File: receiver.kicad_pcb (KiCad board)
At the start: 2 copper layers, 63 x 61 mm, 35 parts, among them J1 Screw_Terminal_01x02, J2 Screw_Terminal_01x02, Q1 BC549, Q2 BC549, U1 AMS1117-3.3

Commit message: Почти готово. Осталось добавить переменный конденсатор
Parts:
- moved C8 56.9 mm to (76.0, 90.1), turned to 0 degrees
- moved C11 53.1 mm to (76.0, 86.0), turned to 0 degrees
- moved D1 51.1 mm to (124.7, 97.8), turned to -90 degrees
- moved C9 39.5 mm to (112.0, 96.6), turned to 90 degrees
- moved R1 37.6 mm to (89.8, 100.4), turned to 180 degrees
- moved C2 35.6 mm to (107.7, 61.2), turned to -90 degrees
- moved C4 35.1 mm to (108.2, 96.8), turned to 180 degrees
- moved D2 25.4 mm to (92.5, 91.0)
- moved C7 23.3 mm to (115.6, 81.5), turned to -90 degrees
- moved R2 23.2 mm to (89.8, 98.0), turned to 0 degrees
- moved D3 23.0 mm to (75.5, 99.4)
- moved C14 22.9 mm to (85.3, 81.7), turned to 180 degrees
- moved C15 22.2 mm to (99.5, 86.3), turned to 0 degrees
- moved C5 19.2 mm to (108.3, 93.3), turned to 180 degrees
- moved C12 15.8 mm to (86.2, 94.0), turned to 180 degrees
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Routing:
- net Net-(D3-K): track 7.52 -> 111.2 mm
- net Net-(C10-Pad1): track 24.7 -> 103.8 mm, vias 0 -> 2
- net Net-(AE1-A): track 15.8 -> 82.4 mm
- net Net-(D1-K): track 21.9 -> 77.2 mm
- net Earth: track 80.8 -> 134.6 mm
- net Net-(C12-Pad1): track 43.4 -> 3.82 mm
- net Net-(D2-input): track 0.00 -> 36.5 mm
- net Net-(D2-MUX): track 18.4 -> 45.8 mm
- net Net-(C7-Pad2): track 0.00 -> 25.9 mm
- net Net-(C13-Pad2): track 33.4 -> 10.0 mm, vias 2 -> 0
- net Net-(D2-OSC): track 16.4 -> 37.4 mm, vias 2 -> 0
- net Net-(C9-Pad2): track 0.00 -> 19.4 mm
- net Net-(C12-Pad2): track 32.0 -> 14.3 mm
- net Net-(D2-fld): track 17.8 -> 8.96 mm
- net +3V3: track 194.6 -> 188.3 mm, vias 0 -> 3
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
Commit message: Почти все. Четыре дорожки внутри микросхемы. Это много.
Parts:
- moved C5 10.1 mm to (98.3, 91.6), turned to 0 degrees
- moved C4 10.1 mm to (98.3, 95.1), turned to 0 degrees
- moved C18 8.39 mm to (111.8, 67.4)
- moved C7 7.28 mm to (116.0, 74.3)
- moved C9 7.28 mm to (112.4, 89.4)
- moved C10 7.25 mm to (108.1, 88.5)
- moved C1 4.55 mm to (119.0, 63.7)
- moved C11 3.08 mm to (75.8, 89.1)
- moved C14 3.08 mm to (85.1, 84.8)
- moved C8 3.08 mm to (75.8, 93.2)
- moved C12 3.08 mm to (86.0, 97.1)
- moved D1 2.57 mm to (124.7, 95.2)
- moved AE1 2.52 mm to (130.6, 100.8)
- moved R4 2.41 mm to (130.3, 60.4)
- moved D4 2.12 mm to (108.6, 54.6)
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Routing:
- net +3V3: track 188.3 -> 212.4 mm, vias 3 -> 4
- net Net-(C7-Pad2): track 25.9 -> 49.8 mm
- net Net-(C10-Pad1): track 103.8 -> 80.7 mm
- net Net-(D3-K): track 111.2 -> 96.0 mm
- net Net-(D1-K): track 77.2 -> 62.3 mm
- net Earth: track 134.6 -> 125.0 mm
- net Net-(J2-Pin_1): track 11.8 -> 18.8 mm
- net Net-(C9-Pad2): track 19.4 -> 25.0 mm
- net Net-(C14-Pad1): track 11.3 -> 6.84 mm
- net Net-(D2-MUX): track 45.8 -> 48.9 mm
- net Net-(D2-OSC): track 37.4 -> 39.9 mm
- net Net-(C12-Pad2): track 14.3 -> 16.6 mm
- net Net-(D2-input): track 36.5 -> 34.6 mm
- net Net-(Q1-B): track 5.72 -> 7.19 mm
- net Net-(C12-Pad1): track 3.82 -> 5.14 mm
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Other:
- outline, holes or cut-outs redrawn

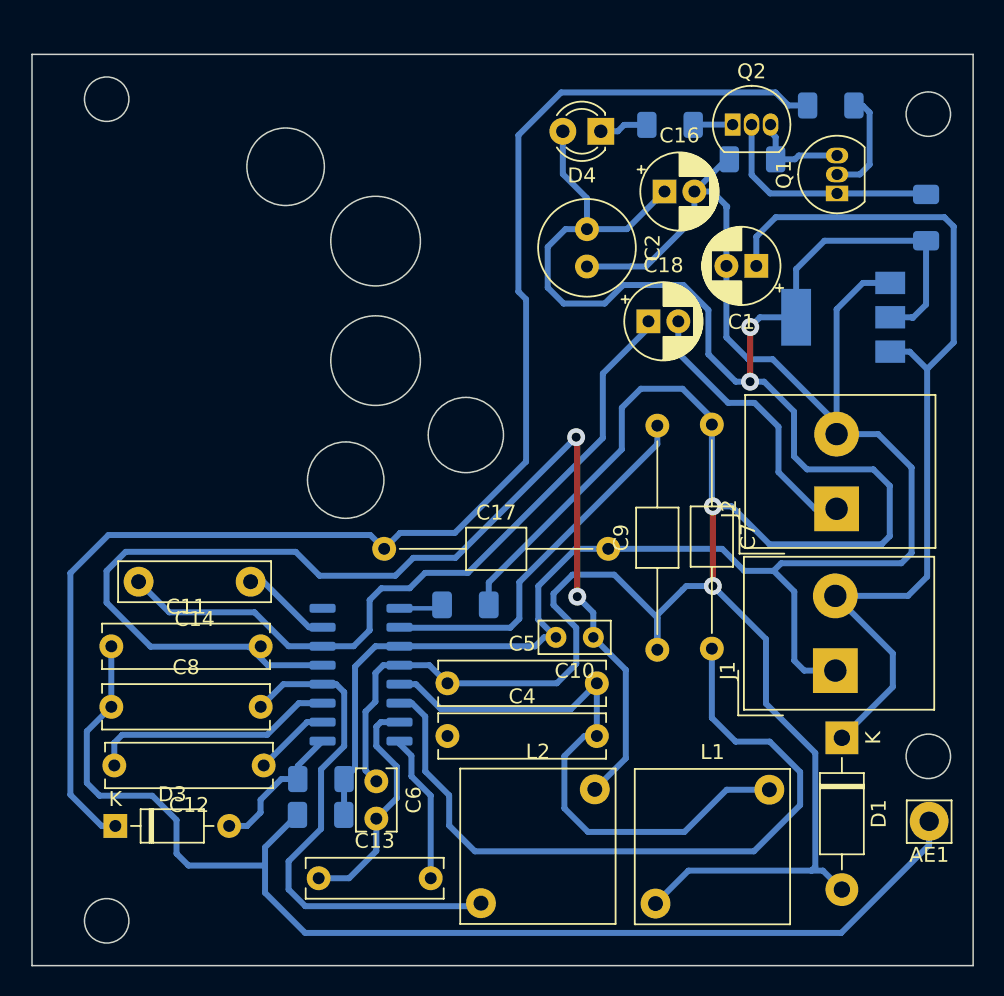
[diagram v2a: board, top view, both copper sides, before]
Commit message: Уменьшена плотность дорожек
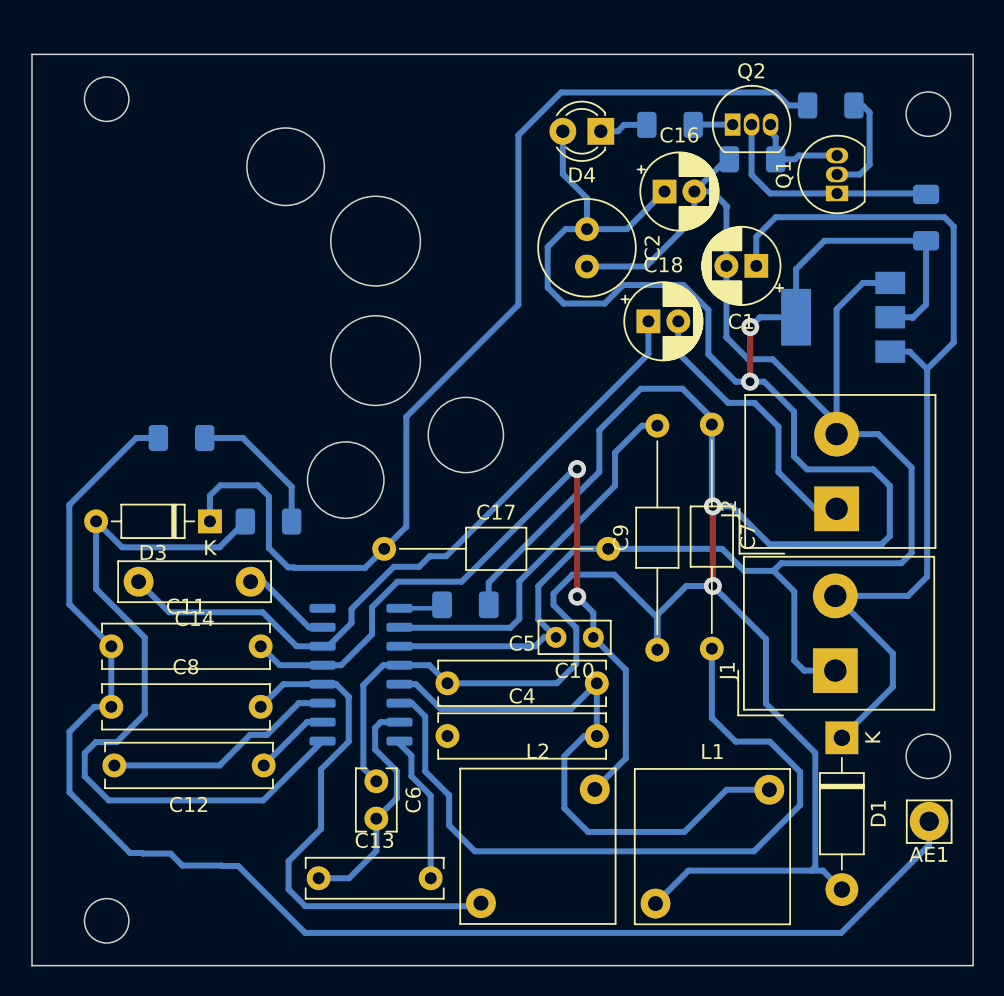
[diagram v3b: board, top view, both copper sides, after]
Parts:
- moved R1 26.9 mm to (80.5, 75.2)
- moved D3 21.3 mm to (82.4, 80.8), turned to 180 degrees
- moved R2 17.6 mm to (86.3, 80.8)
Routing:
- net Net-(D2-fld): track 9.62 -> 50.6 mm
- net Net-(C10-Pad1): track 80.7 -> 52.0 mm
- net Net-(D3-K): track 96.0 -> 70.8 mm
- net Net-(AE1-A): track 81.1 -> 95.5 mm
- net Earth: track 125.0 -> 120.7 mm
- net Net-(D2-MUX): track 48.9 -> 46.8 mm
- net Net-(C12-Pad2): track 16.6 -> 15.7 mm
- net Net-(C9-Pad2): track 25.0 -> 25.6 mm

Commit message: Теперь только три дорожки между ножками микросхемы.
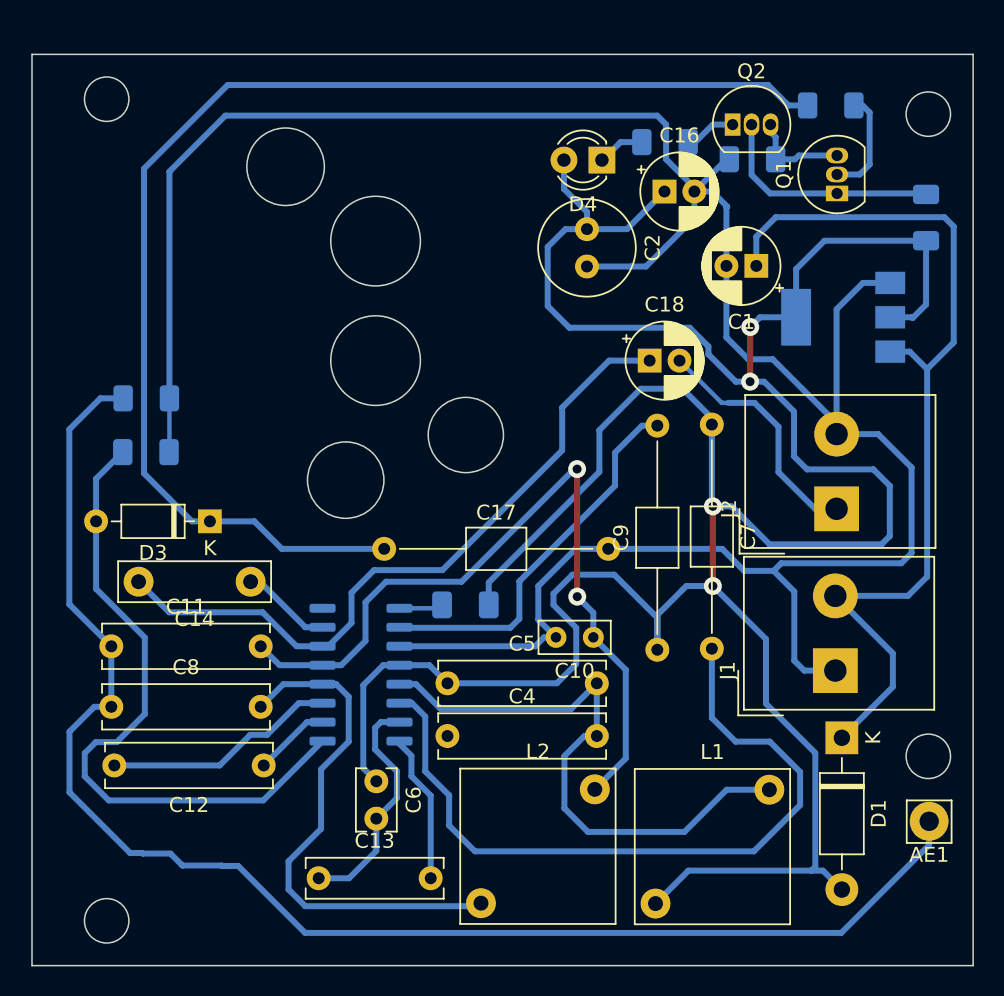
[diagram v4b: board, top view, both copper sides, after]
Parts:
- moved R2 9.43 mm to (78.1, 76.1)
- moved R1 3.55 mm to (78.2, 72.5)
- moved C18 2.63 mm to (111.8, 70.0)
- moved D4 1.93 mm to (108.7, 56.6)
- moved R6 1.20 mm to (112.9, 55.4)
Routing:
- net Earth: track 120.7 -> 170.3 mm
- net Net-(D3-K): track 70.8 -> 85.9 mm
- net Net-(D2-fld): track 50.6 -> 44.5 mm
- net +3V3: track 212.6 -> 208.9 mm
- net Net-(J2-Pin_1): track 18.8 -> 16.4 mm
- net Net-(AE1-A): track 95.5 -> 97.2 mm
- net Net-(Q2-C): track 2.65 -> 3.46 mm

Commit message: Добавлена SMD-индуктивность.
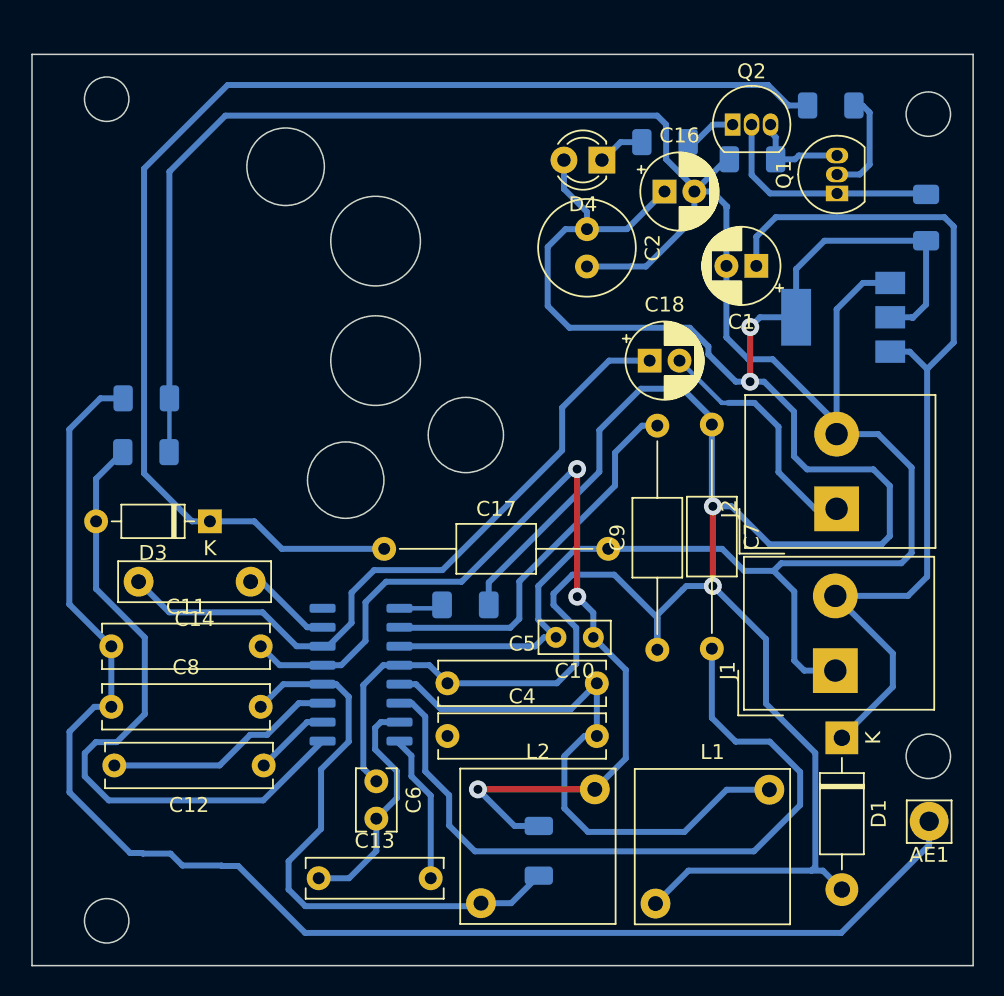
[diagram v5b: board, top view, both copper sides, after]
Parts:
- added L3: L, Inductor_SMD:L_1206_3216Metric_Pad1.22x1.90mm_HandSolder, B.Cu at (104.4, 102.8)
- C17, C7, C9: footprint Capacitor_THT:C_Axial_L3.8mm_D2.6mm_P15.00mm_Horizontal -> Capacitor_THT:C_Axial_L5.1mm_D3.1mm_P15.00mm_Horizontal
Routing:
- net Net-(C10-Pad1): track 52.3 -> 65.2 mm, vias 2 -> 3
- net Net-(D2-input): track 34.9 -> 39.5 mm

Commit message: Добавлено посадочное место для переменного конденсатора.
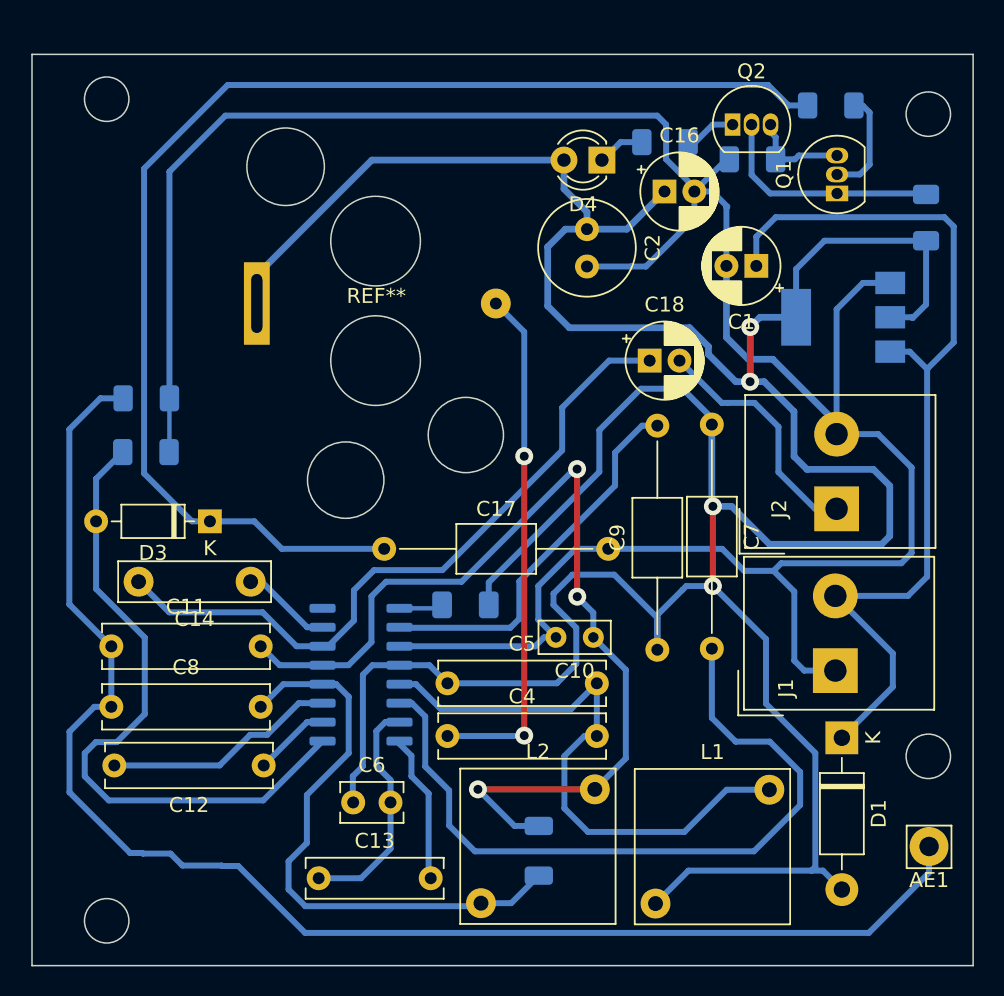
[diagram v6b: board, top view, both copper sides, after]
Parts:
- added REF**: Capasitor_Variable, my_library:Capasitor_Variable, F.Cu at (93.5, 66.2)
- moved C6 2.10 mm to (92.0, 99.6), turned to 0 degrees
- moved AE1 1.69 mm to (130.6, 102.5)
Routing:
- net Net-(C3-Pad2): track 0.00 -> 34.8 mm, vias 0 -> 2
- net +3V3: track 208.9 -> 236.3 mm
- net Net-(AE1-A): track 97.2 -> 96.6 mm

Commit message: посадочные места катушек индуктивности размещены по местам. вроде бы,все готово к производству.
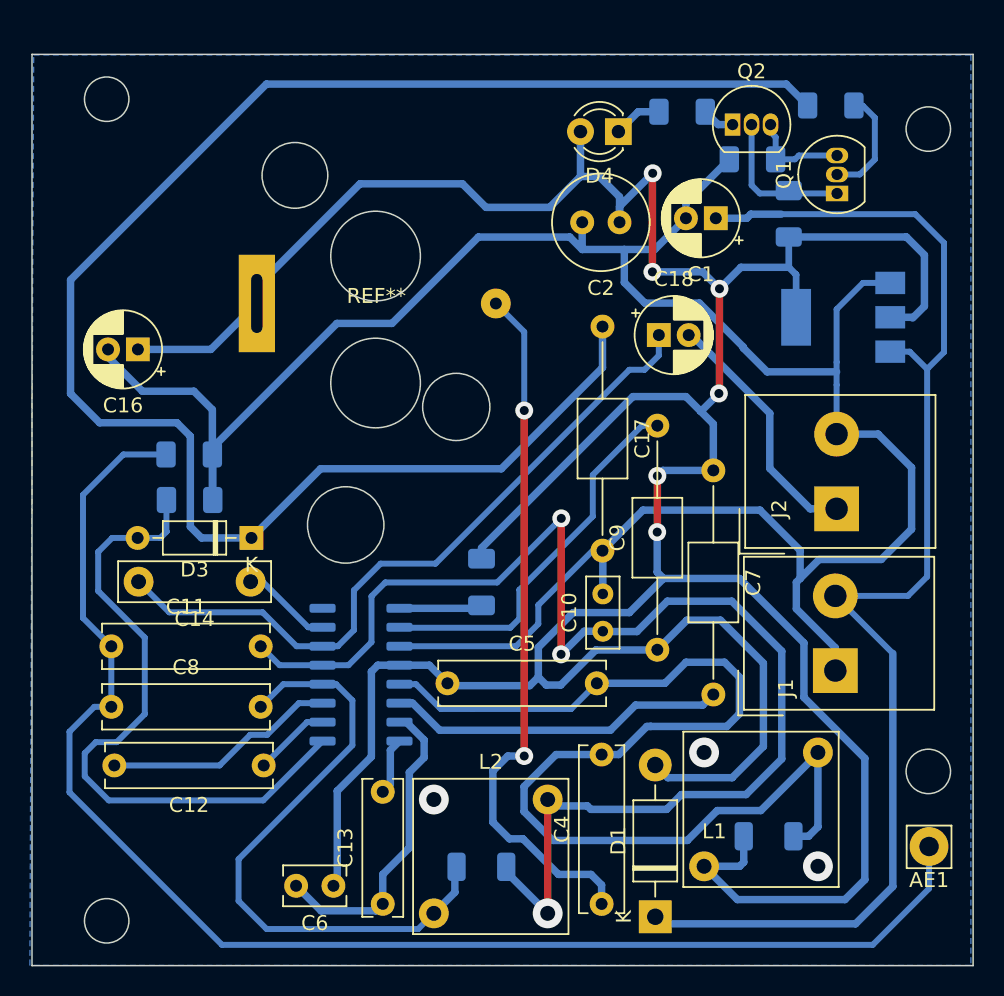
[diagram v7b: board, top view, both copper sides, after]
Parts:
- added L4: L, Inductor_SMD:L_1206_3216Metric_Pad1.22x1.90mm_HandSolder, B.Cu at (119.8, 101.8)
- moved C16 36.8 mm to (77.6, 69.2), turned to 180 degrees
- moved C17 20.9 mm to (108.7, 67.7), turned to -90 degrees
- moved D1 17.3 mm to (112.2, 107.2), turned to 90 degrees
- moved C4 15.3 mm to (108.6, 106.4), turned to 90 degrees
- moved R4 9.20 mm to (121.2, 60.2)
- moved C6 5.74 mm to (90.7, 105.2), turned to 180 degrees
- moved R1 4.73 mm to (81.0, 76.3)
- moved C13 4.62 mm to (94.0, 106.4), turned to 90 degrees
- moved R2 4.34 mm to (81.0, 79.3)
- moved C1 4.19 mm to (116.3, 60.5)
- moved L1 4.10 mm to (115.5, 103.8)
- moved L3 3.99 mm to (100.6, 103.9), turned to 0 degrees
- moved L2 3.23 mm to (97.4, 107.0)
- moved C7 3.07 mm to (116.1, 77.3)
- moved D3 2.99 mm to (85.2, 81.9)
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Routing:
- net Net-(D2-OSC): track 39.9 -> 75.7 mm
- net Net-(D3-K): track 85.9 -> 113.6 mm
- net Net-(C7-Pad2): track 49.8 -> 22.8 mm
- net Net-(D1-K): track 62.3 -> 86.8 mm
- net Net-(C10-Pad1): track 65.5 -> 89.7 mm
- net Net-(C3-Pad2): track 34.8 -> 47.3 mm
- net +3V3: track 236.3 -> 248.1 mm, vias 4 -> 6
- net Earth: track 170.3 -> 159.7 mm
- net Net-(C13-Pad2): track 10.0 -> 3.86 mm
- net Net-(Q1-C): track 15.6 -> 10.0 mm
- net Net-(C13-Pad1): track 15.7 -> 21.0 mm
- net Net-(C15-Pad1): track 2.95 -> 5.57 mm
- net Net-(D2-input): track 39.5 -> 41.8 mm
- net Net-(Q2-C): track 3.46 -> 2.19 mm
- net Net-(AE1-A): track 96.6 -> 95.3 mm
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- added copper zone on B.Cu, net Earth
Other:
- outline, holes or cut-outs redrawn

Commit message: немного отодвинул дорохки от отверстий крепления и утолщил дорожки.
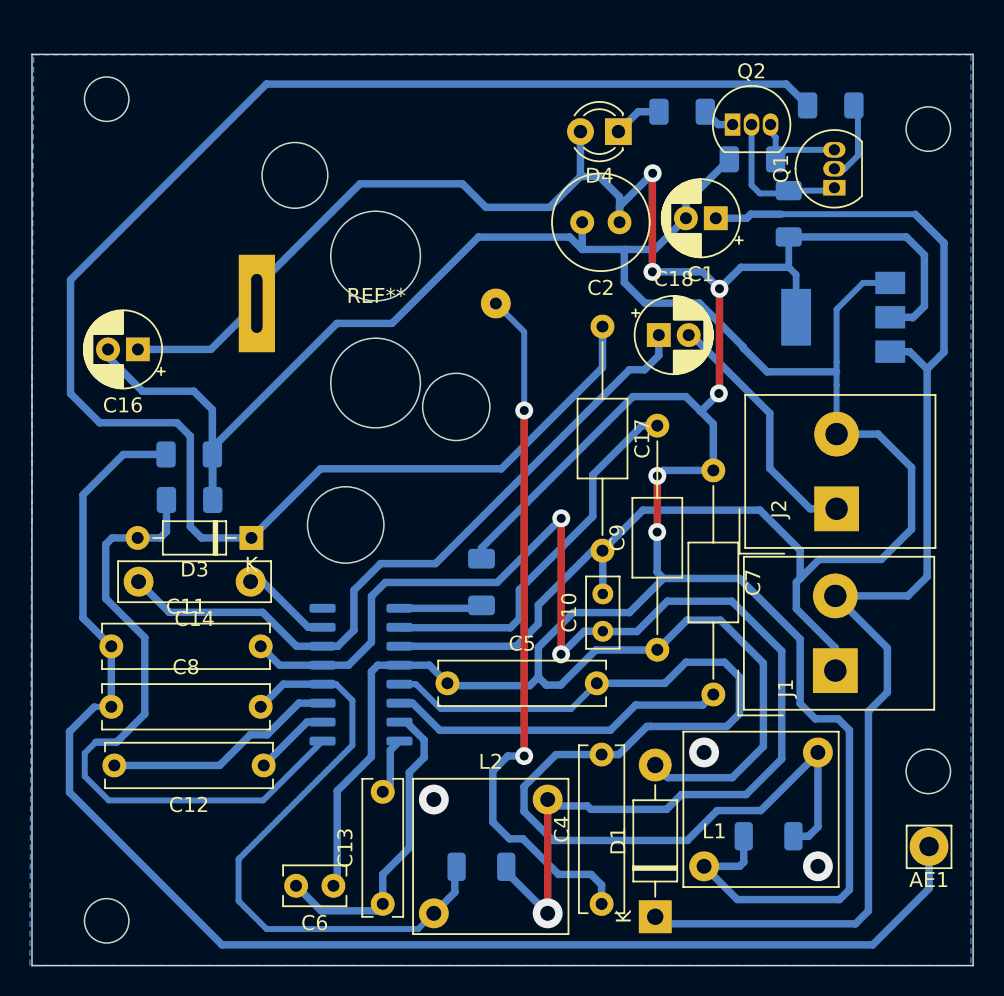
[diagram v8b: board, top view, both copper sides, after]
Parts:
- moved Q1 0.42 mm to (124.2, 58.4)
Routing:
- net Net-(Q1-B): track 7.48 -> 5.42 mm
